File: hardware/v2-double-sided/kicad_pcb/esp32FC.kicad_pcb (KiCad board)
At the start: 2 copper layers, 96.2 x 68.7 mm, 28 parts, among them J1 Conn_01x05_Pin, J10 Screw_Terminal_01x02, J11 Screw_Terminal_01x02, J12 Screw_Terminal_01x02, J2 Conn_01x04_Pin, J3 Conn_01x03_Pin, J4 Conn_01x03_Pin, J5 Conn_01x03_Pin, J6 Conn_01x03_Pin, J7 Screw_Terminal_01x02, J8 Screw_Terminal_01x02, J9 Screw_Terminal_01x02, Q1 2N3904, U1 esp32-wemos-d1-mini

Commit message: Added screw holes and export files
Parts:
- added REF**: MountingHole_3.2mm_M3, MountingHole:MountingHole_3.2mm_M3, F.Cu at (125.8, 127.5)
- added REF**: MountingHole_3.2mm_M3, MountingHole:MountingHole_3.2mm_M3, F.Cu at (171.1, 127.5)
- added REF**: MountingHole_3.2mm_M3, MountingHole:MountingHole_3.2mm_M3, F.Cu at (112.3, 82.5)
- added REF**: MountingHole_3.2mm_M3, MountingHole:MountingHole_3.2mm_M3, F.Cu at (184.6, 82.5)
- moved J10 9.90 mm to (114.6, 90.2)
- moved J11 9.89 mm to (182.8, 90.2)
- moved J8 4.88 mm to (114.5, 127.6)
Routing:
- net GNDPWR: track 281.0 -> 245.6 mm
- net GND: track 293.7 -> 291.7 mm
- net +BATT: track 316.4 -> 316.9 mm, vias 0 -> 1

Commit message: Modified connectors for serial connections, now used molex connectors
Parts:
- J1: value Conn_01x05_Pin -> Conn_01x06_Pin; footprint Connector_PinHeader_2.54mm:PinHeader_1x05_P2.54mm_Vertical -> Connector_Molex:Molex_KK-254_AE-6410-06A_1x06_P2.54mm_Vertical
- J2: footprint Connector_PinHeader_2.54mm:PinHeader_1x04_P2.54mm_Vertical -> Connector_Molex:Molex_KK-254_AE-6410-04A_1x04_P2.54mm_Vertical
- moved J1 12.8 mm to (125.5, 96.5), turned to 90 degrees
- moved J2 7.71 mm to (125.5, 79.9), turned to 90 degrees
- moved R3 0.53 mm to (118.2, 75.0)
- moved Q1 0.41 mm to (174.1, 87.4)
- moved J3 0.06 mm to (168.6, 83.4)
- moved J4 0.06 mm to (168.6, 79.4)
- moved J5 0.06 mm to (168.6, 75.4)
- moved J6 0.06 mm to (168.6, 71.4)
- renumbered C6 to C3, C7 to C4, C3 to C5, C4 to C6, C5 to C7, J7 to J12, J12 to J7, R3 to R2, R4 to R3
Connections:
- J1 pad 1: RX3 -> unconnected-(J1-Pin_1-Pad1)
- J1 pad 2: TX3 -> +5V
- J1 pad 3: +3.3V -> GND
- J1 pad 4: GND -> +3.3V
- J1 pad 5: +5V -> TX3
- J2 pad 1: GND -> TX2
- J2 pad 2: +5V -> RX2
- J2 pad 3: RX2 -> +5V
- J2 pad 4: TX2 -> GND
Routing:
- net +5V: track 177.7 -> 155.0 mm
- net GND: track 291.7 -> 298.2 mm, vias 6 -> 5
- net +3.3V: track 75.1 -> 69.6 mm

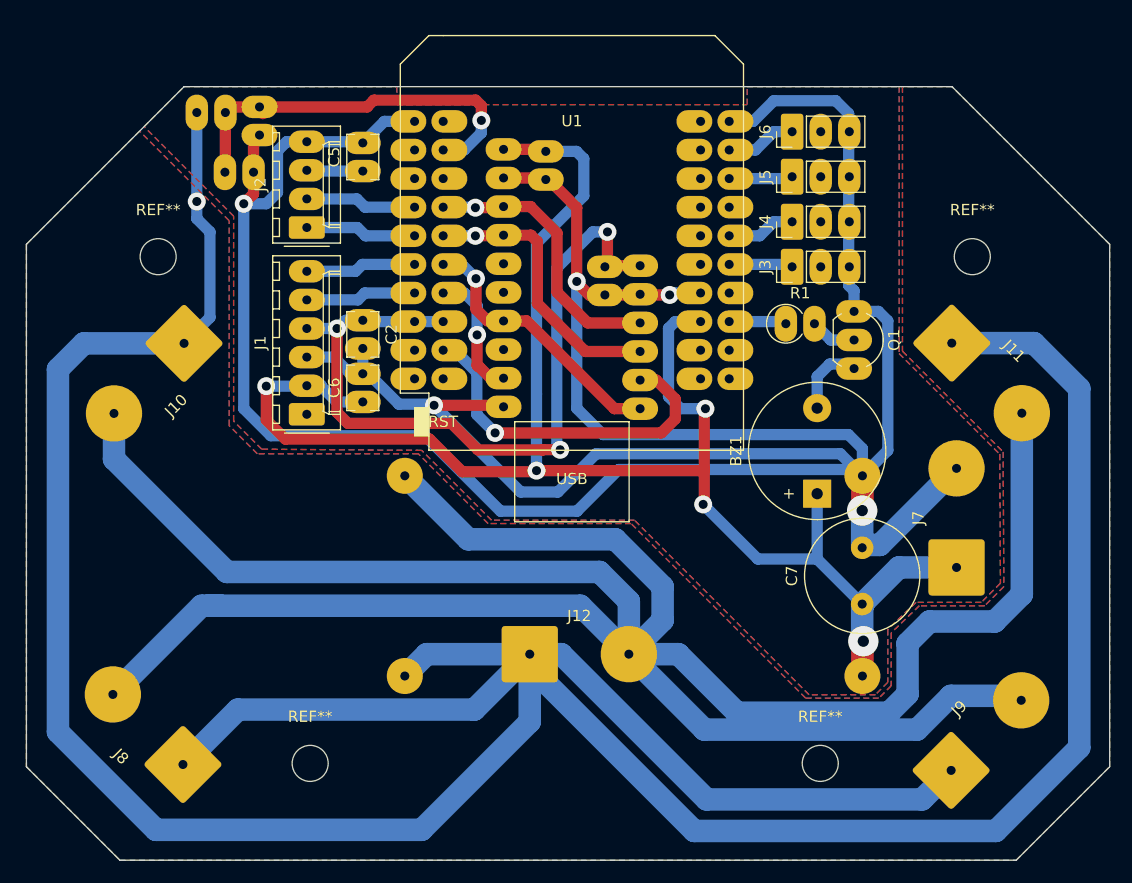
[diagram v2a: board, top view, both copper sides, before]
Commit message: Modified the PCB so it now has two ground layers instead of one power and one ground.
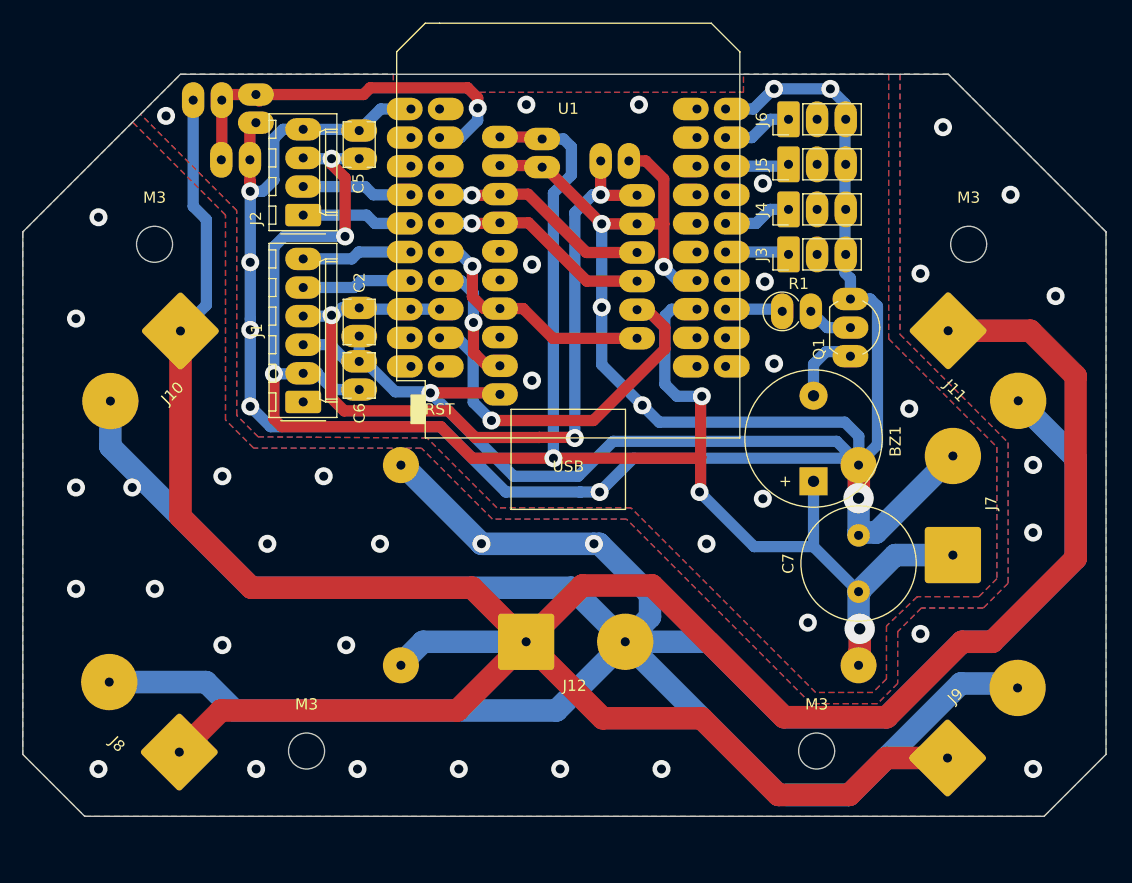
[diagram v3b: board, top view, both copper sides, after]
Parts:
- moved C3 9.41 mm to (151.6, 74.0), turned to 0 degrees
- moved U3 6.26 mm to (150.4, 72.0)
- moved R2 1.15 mm to (115.4, 68.6)
- moved C1 1.15 mm to (121.0, 68.1)
- moved C2 1.15 mm to (130.2, 87.0)
- moved C4 1.15 mm to (146.4, 72.0)
- moved C5 1.15 mm to (130.2, 73.8)
- moved C6 1.15 mm to (130.2, 94.3)
- moved J10 1.15 mm to (114.3, 89.1)
- moved J3 1.15 mm to (168.3, 82.3)
- moved J4 1.15 mm to (168.3, 78.3)
- moved J5 1.15 mm to (168.3, 74.3)
- moved J6 1.15 mm to (168.3, 70.3)
- moved J12 1.15 mm to (145.0, 116.7)
- moved J1 1.15 mm to (125.2, 95.4)
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- renumbered REF** to M3
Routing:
- net +BATT: track 316.9 -> 257.4 mm, vias 1 -> 0
- net +5V: track 155.0 -> 176.3 mm, vias 5 -> 7
- net GNDPWR: track 245.6 -> 254.0 mm, vias 0 -> 28
- net SCK/SCL: track 25.4 -> 19.7 mm
- net SDA/SDI-MOSI: track 25.5 -> 19.8 mm
- net SA0/SD0/AD0-MISO: track 24.9 -> 22.3 mm
- net GND: track 298.2 -> 300.6 mm, vias 5 -> 25
- net +3.3V: track 69.6 -> 71.8 mm
- net NCS: track 31.4 -> 33.3 mm
- net TX2: track 8.41 -> 9.88 mm
- added copper zone on F.Cu, net GND
- added copper zone on F.Cu, net GNDPWR
- removed copper zone on F.Cu, net +5V
- removed copper zone on F.Cu, net +BATT
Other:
- board size 96.2 x 68.7 mm -> 96.2 x 65.9 mm

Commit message: Added two additional outs, to connect two additional servos
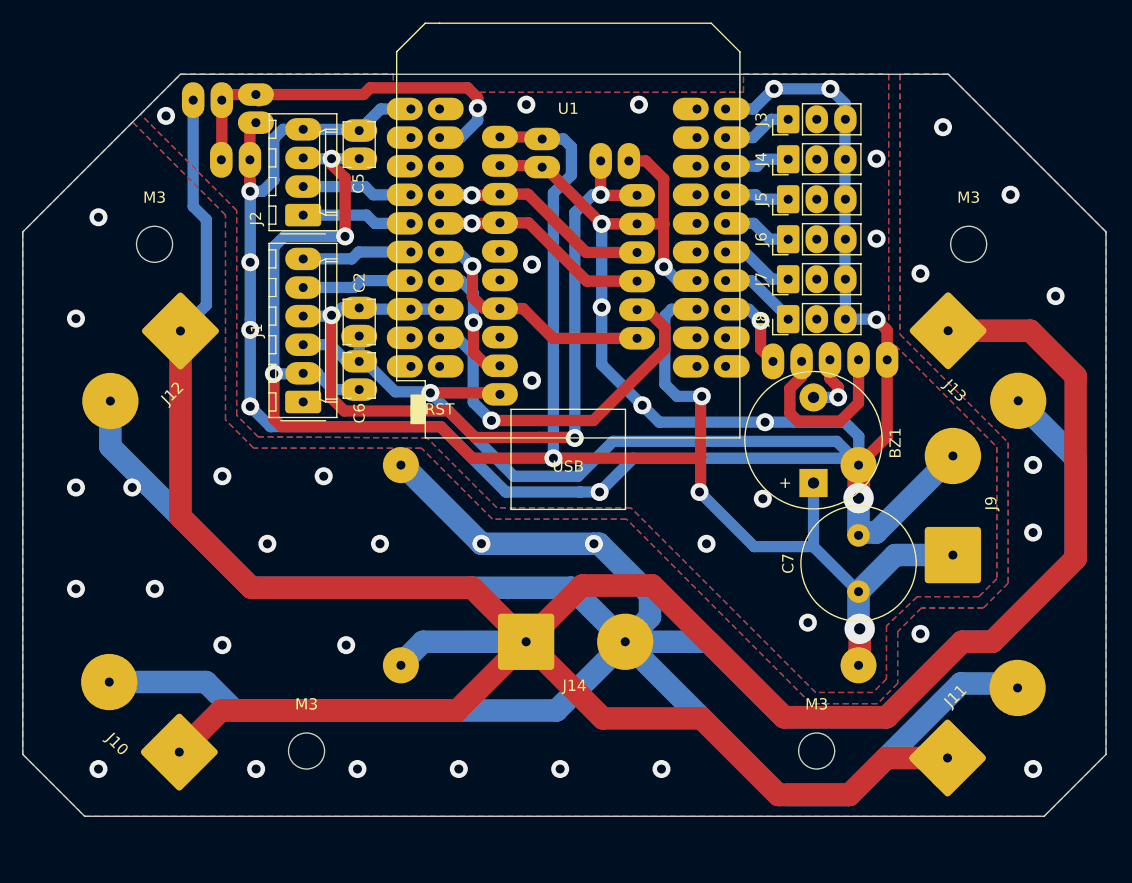
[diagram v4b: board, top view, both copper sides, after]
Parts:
- added J7: Conn_01x03_Pin, Connector_PinHeader_2.54mm:PinHeader_1x03_P2.54mm_Vertical, F.Cu at (168.2, 84.5)
- added J8: Conn_01x03_Pin, Connector_PinHeader_2.54mm:PinHeader_1x03_P2.54mm_Vertical, F.Cu at (168.2, 88.0)
- Q1: moved to B.Cu
- R3: renamed from R1; moved to B.Cu
- moved J3 12.0 mm to (168.2, 70.3)
- moved J6 10.7 mm to (168.2, 81.0)
- moved Q1 6.31 mm to (177.0, 91.7), turned to 180 degrees
- moved R3 4.52 mm to (166.9, 91.8)
- moved J4 4.45 mm to (168.2, 73.8)
- moved J5 3.10 mm to (168.2, 77.4)
- moved BZ1 0.15 mm to (170.5, 102.6)
- renumbered J8 to J10, J9 to J11, J10 to J12, J11 to J13, J12 to J14, J7 to J9, R2 to R1, R3 to R2
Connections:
- J3 pad 1: M3 -> M1
- J4 pad 1: M4 -> M2
- J5 pad 1: M2 -> M3
- J6 pad 1: M1 -> M4
- U1 pad 28: unconnected-(U1-IO_32-Pad28) -> M3
- U1 pad 32: M3 -> SERVO1
- U1 pad 34: unconnected-(U1-IO_00-Pad34) -> SERVO2
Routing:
- net Net-(Q1-B): track 4.12 -> 15.9 mm
- net SERVO2: track 0.00 -> 7.07 mm
- net SERVO1: track 0.00 -> 6.56 mm
- net Buzzer: track 5.11 -> 7.59 mm, vias 0 -> 1
- net GND: track 300.6 -> 301.5 mm
- net Net-(BZ1--): track 6.48 -> 5.83 mm, vias 0 -> 1
